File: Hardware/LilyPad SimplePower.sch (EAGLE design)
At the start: 22 parts, among them U1 MCP73831

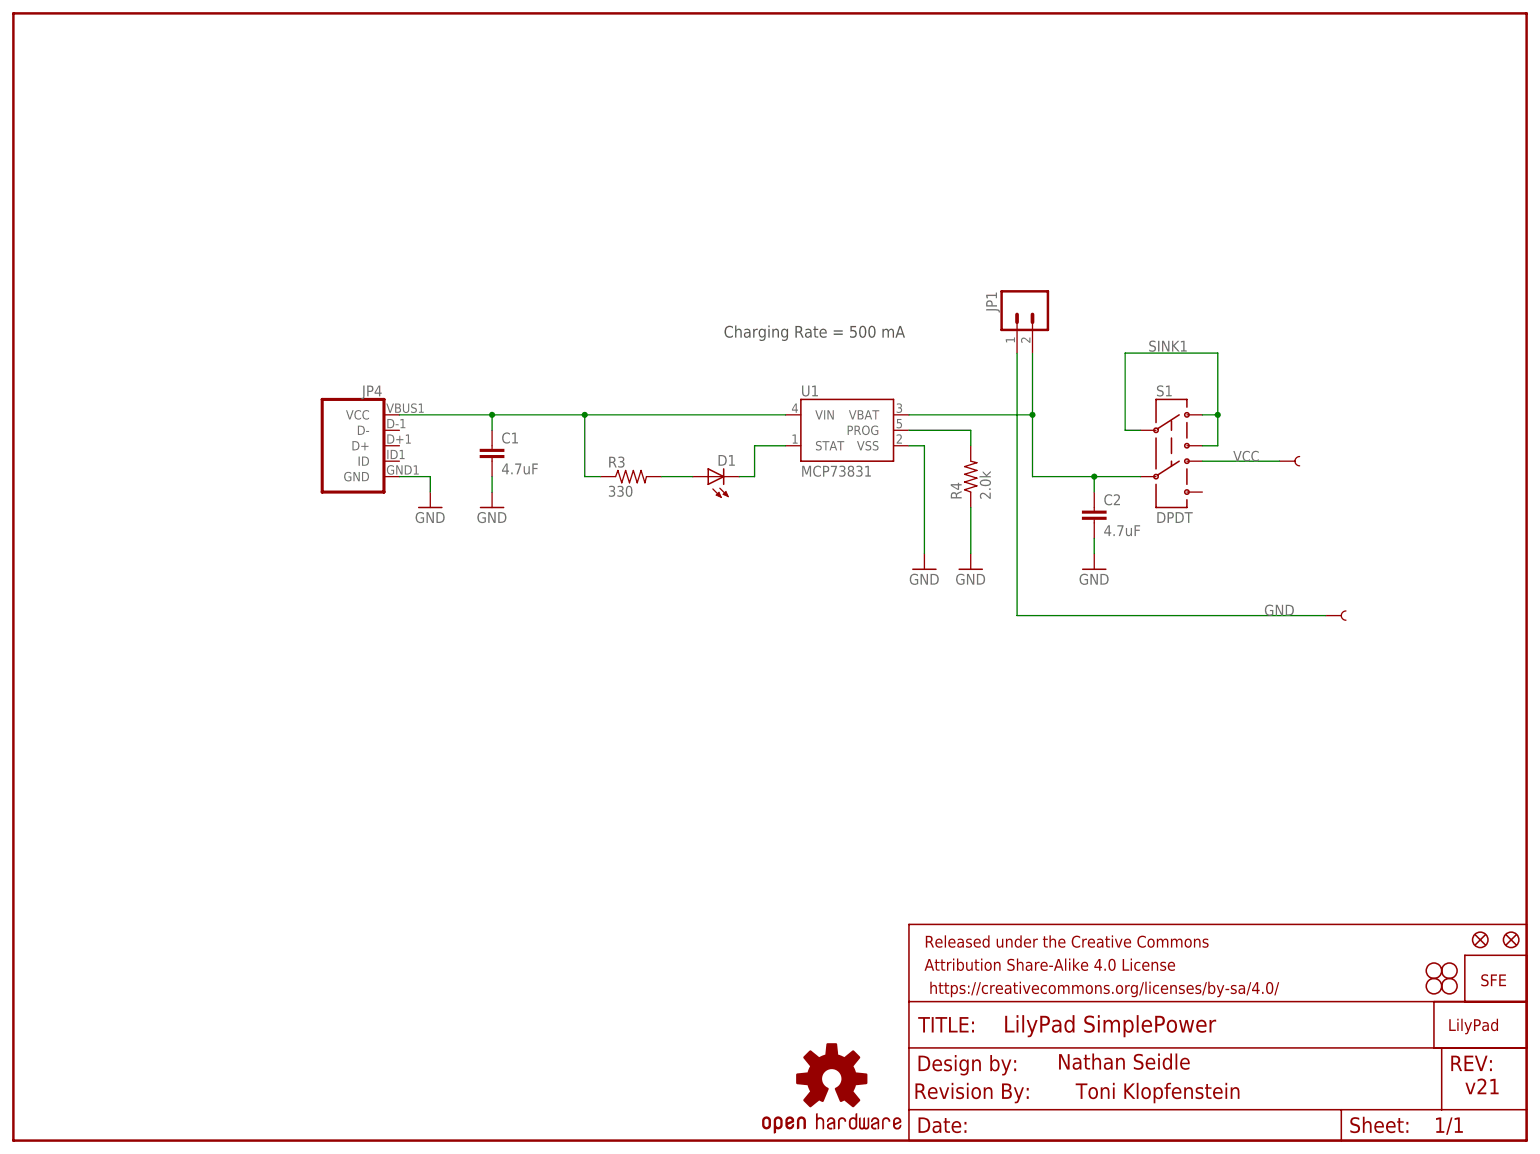
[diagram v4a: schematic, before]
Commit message: Fixing QC issues
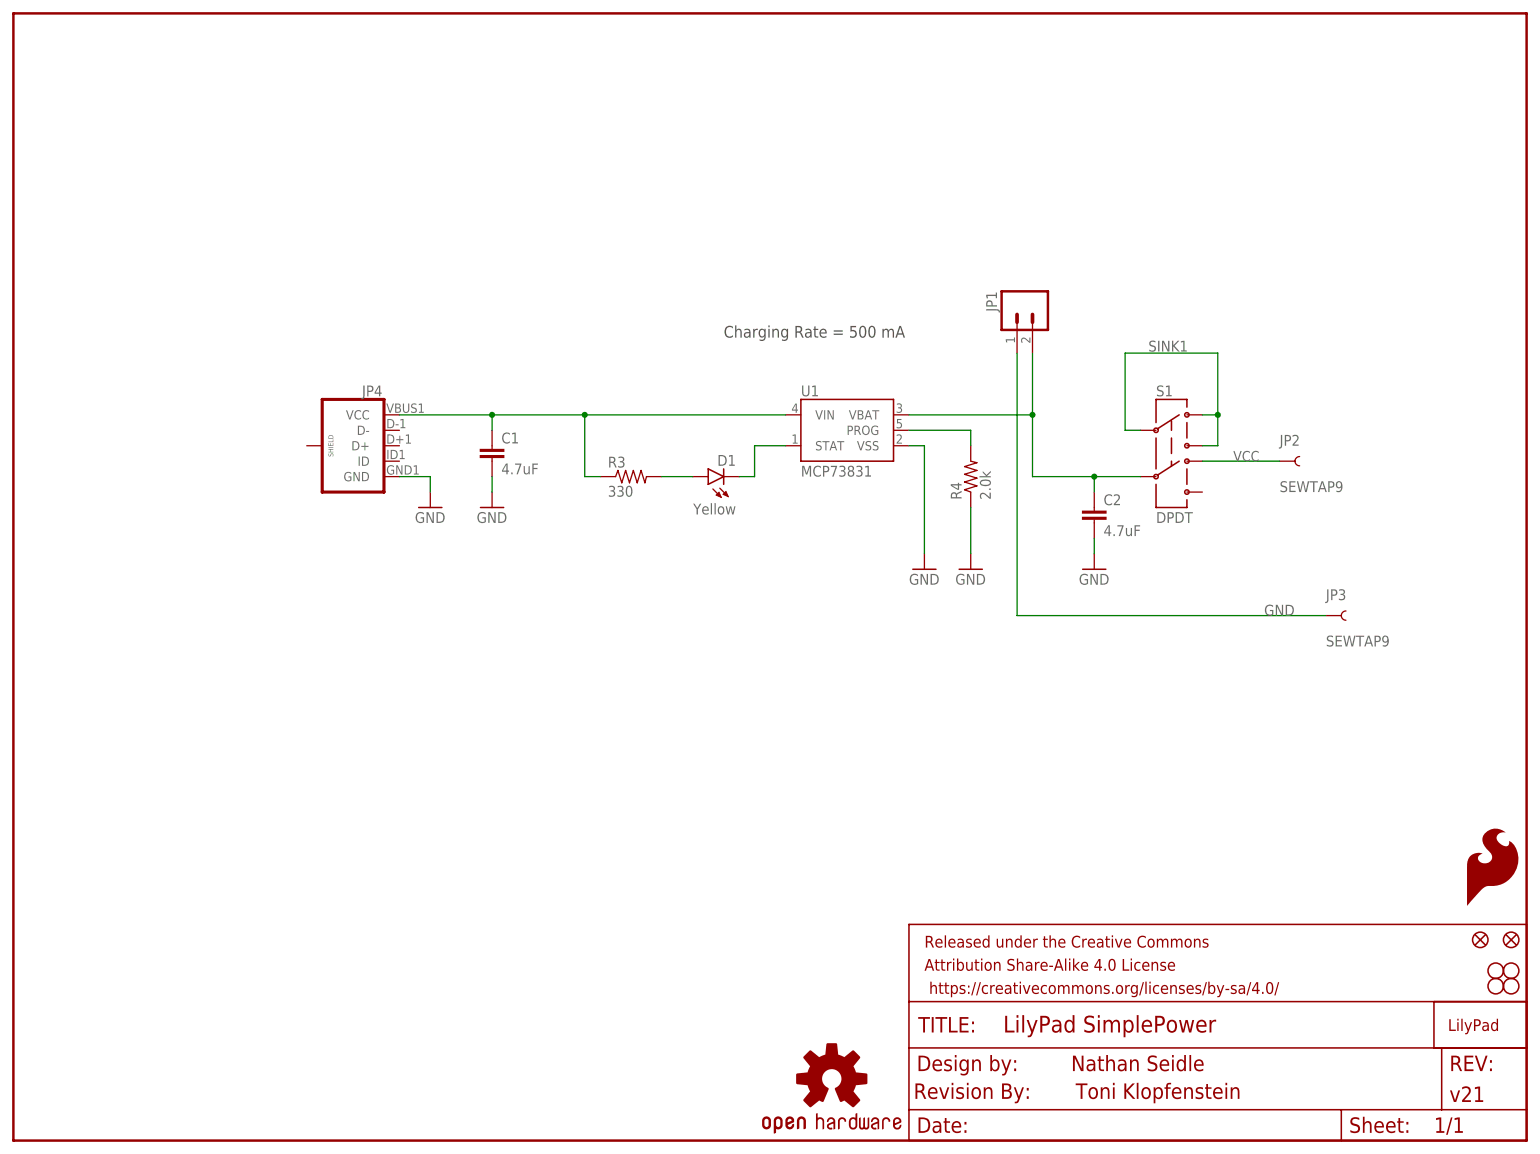
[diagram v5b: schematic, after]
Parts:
- removed U$3: SEWTAP9, LilyPad-Wearables:SEWTAP9
- added JP5: SFE_LOGO_FLAME.1_INCH, SparkFun-Aesthetics:SFE_LOGO_FLAME.1_INCH
- D1: value (none) -> Yellow
- FRAME1: value FRAME-LETTER -> (none); DESIGNER (none) -> Nathan Seidle; VERSION (none) -> v21
- JP3: value LOGO-SFESK -> SEWTAP9; device SparkFun-Aesthetics:LOGO-SFESK -> LilyPad-Wearables:SEWTAP9
- renumbered U$4 to JP2
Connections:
- net GND: now also JP3.1; no longer U$3.1
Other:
- note removed: "Nathan Seidle"
- note removed: "v21"
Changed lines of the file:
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@@
 <layer number="251" name="SMDround" color="12" fill="11" visible="no" active="no"/>
 <layer number="254" name="cooling" color="7" fill="1" visible="yes" active="yes"/>
+<layer number="255" name="routoute" color="7" fill="1" visible="yes" active="yes"/>
 </layers>
 <schematic xreflabel="%F%N/%S" xrefpart="/%S.%C%R">
@@
 </classes>
 <parts>
-<part name="FRAME1" library="SparkFun-Aesthetics" deviceset="FRAME-LETTER" device=""/>
+<part name="FRAME1" library="SparkFun-Aesthetics" deviceset="FRAME-LETTER" device="">
+<attribute name="DESIGNER" value="Nathan Seidle"/>
+<attribute name="VERSION" value="v21"/>
+</part>
 <part name="S1" library="SparkFun-Electromechanical" deviceset="SWITCH-DPDT" device="AYZ0202" value="DPDT"/>
 <part name="JP1" library="SparkFun-Connectors" deviceset="M02" device="-JST-2MM-SMT"/>
-<part name="U$3" library="LilyPad-Wearables" deviceset="SEWTAP" device="9" value="SEWTAP9"/>
-<part name="U$4" library="LilyPad-Wearables" deviceset="SEWTAP" device="9" value="SEWTAP9"/>
+<part name="JP3" library="LilyPad-Wearables" deviceset="SEWTAP" device="9" value="SEWTAP9"/>
+<part name="JP2" library="LilyPad-Wearables" deviceset="SEWTAP" device="9" value="SEWTAP9"/>
 <part name="U$5" library="SparkFun-Aesthetics" deviceset="OSHW-LOGO" device="S"/>
-<part name="JP3" library="SparkFun-Aesthetics" deviceset="LOGO-SFE" device="SK"/>
+<part name="JP5" library="SparkFun-Aesthetics" deviceset="SFE_LOGO_FLAME" device=".1_INCH"/>
 <part name="U1" library="SparkFun-PowerIC" deviceset="MCP73831" device=""/>
 <part name="JP4" library="SparkFun-Connectors" deviceset="USB_MICROB_PLUG" device="CONN-11752"/>
@@
 <part name="GND2" library="SparkFun-Aesthetics" deviceset="GND" device=""/>
 <part name="R3" library="SparkFun-Resistors" deviceset="330OHM1/10W1%(0603)" device="" value="330"/>
-<part name="D1" library="SparkFun-LED" deviceset="LED-YELLOW" device="0603"/>
+<part name="D1" library="SparkFun-LED" deviceset="LED-YELLOW" device="0603" value="Yellow"/>
 <part name="C2" library="SparkFun-Capacitors" deviceset="4.7UF-6.3V-10%(0603)" device="0603" value="4.7uF"/>
 <part name="GND3" library="SparkFun-Aesthetics" deviceset="GND" device=""/>
@@
 <sheet>
 <plain>
-<text x="171.704" y="11.684" size="2.54" layer="94">Nathan Seidle</text>
-<text x="238.76" y="7.62" size="2.54" layer="94">v21</text>
 <text x="174.752" y="6.858" size="2.54" layer="94">Toni Klopfenstein</text>
 <text x="116.84" y="132.08" size="1.9304" layer="97">Charging Rate = 500 mA</text>
@@
 <instances>
 <instance part="FRAME1" gate="G$1" x="0" y="0"/>
-<instance part="FRAME1" gate="G$2" x="147.32" y="0"/>
+<instance part="FRAME1" gate="V" x="147.32" y="0"/>
 <instance part="S1" gate="G$1" x="190.5" y="114.3"/>
 <instance part="JP1" gate="G$1" x="167.64" y="137.16" smashed="yes" rot="MR270">
 <attribute name="NAME" x="161.798" y="139.7" size="1.778" layer="95" rot="MR270"/>
 </instance>
-<instance part="U$3" gate="G$1" x="218.44" y="86.36"/>
-<instance part="U$4" gate="G$1" x="210.82" y="111.76"/>
+<instance part="JP3" gate="G$1" x="218.44" y="86.36"/>
+<instance part="JP2" gate="G$1" x="210.82" y="111.76"/>
 <instance part="U$5" gate="G$1" x="134.62" y="10.16"/>
-<instance part="JP3" gate="G$1" x="241.3" y="25.4"/>
+<instance part="JP5" gate="G$1" x="238.76" y="38.1"/>
 <instance part="U1" gate="G$1" x="137.16" y="116.84"/>
 <instance part="JP4" gate="G$1" x="55.88" y="114.3" smashed="yes" rot="MR0">
@@
 <instance part="GND2" gate="1" x="78.74" y="104.14"/>
 <instance part="R3" gate="G$1" x="101.6" y="109.22"/>
-<instance part="D1" gate="G$1" x="114.3" y="109.22" rot="R90"/>
+<instance part="D1" gate="G$1" x="114.3" y="109.22" smashed="yes" rot="R90">
+<attribute name="NAME" x="118.872" y="112.776" size="1.778" layer="95" rot="R180"/>
+<attribute name="VALUE" x="118.872" y="104.775" size="1.778" layer="96" rot="R180"/>
+</instance>
 <instance part="C2" gate="G$1" x="177.8" y="101.6"/>
 <instance part="GND3" gate="1" x="149.86" y="93.98"/>
@@
 <instance part="U$6" gate="G$1" x="148.082" y="6.858"/>
 <instance part="U$1" gate="G$1" x="236.22" y="17.78"/>
-<instance part="STANDOFF1" gate="G$1" x="236.22" y="27.94"/>
-<instance part="STANDOFF2" gate="G$1" x="233.68" y="27.94"/>
-<instance part="STANDOFF3" gate="G$1" x="233.68" y="25.4"/>
-<instance part="STANDOFF4" gate="G$1" x="236.22" y="25.4"/>
+<instance part="STANDOFF1" gate="G$1" x="246.38" y="27.94"/>
+<instance part="STANDOFF2" gate="G$1" x="243.84" y="27.94"/>
+<instance part="STANDOFF3" gate="G$1" x="243.84" y="25.4"/>
+<instance part="STANDOFF4" gate="G$1" x="246.38" y="25.4"/>
 <instance part="FID1" gate="G$1" x="246.38" y="33.02"/>
 <instance part="FID2" gate="G$1" x="241.3" y="33.02"/>
@@
 <wire x1="165.1" y1="86.36" x2="215.9" y2="86.36" width="0.1524" layer="91"/>
 <label x="205.74" y="86.36" size="1.778" layer="95"/>
-<pinref part="U$3" gate="G$1" pin="1"/>
+<pinref part="JP3" gate="G$1" pin="1"/>
 <pinref part="JP1" gate="G$1" pin="2"/>
 <wire x1="165.1" y1="86.36" x2="165.1" y2="129.54" width="0.1524" layer="91"/>
@@
 <wire x1="195.58" y1="111.76" x2="208.28" y2="111.76" width="0.1524" layer="91"/>
 <pinref part="S1" gate="G$1" pin="4"/>
-<pinref part="U$4" gate="G$1" pin="1"/>
+<pinref part="JP2" gate="G$1" pin="1"/>
 <label x="200.66" y="111.76" size="1.6764" layer="95"/>
 </segment>
